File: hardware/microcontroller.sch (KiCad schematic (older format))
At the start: 9 parts, among them U1 ESP-WROOM-32

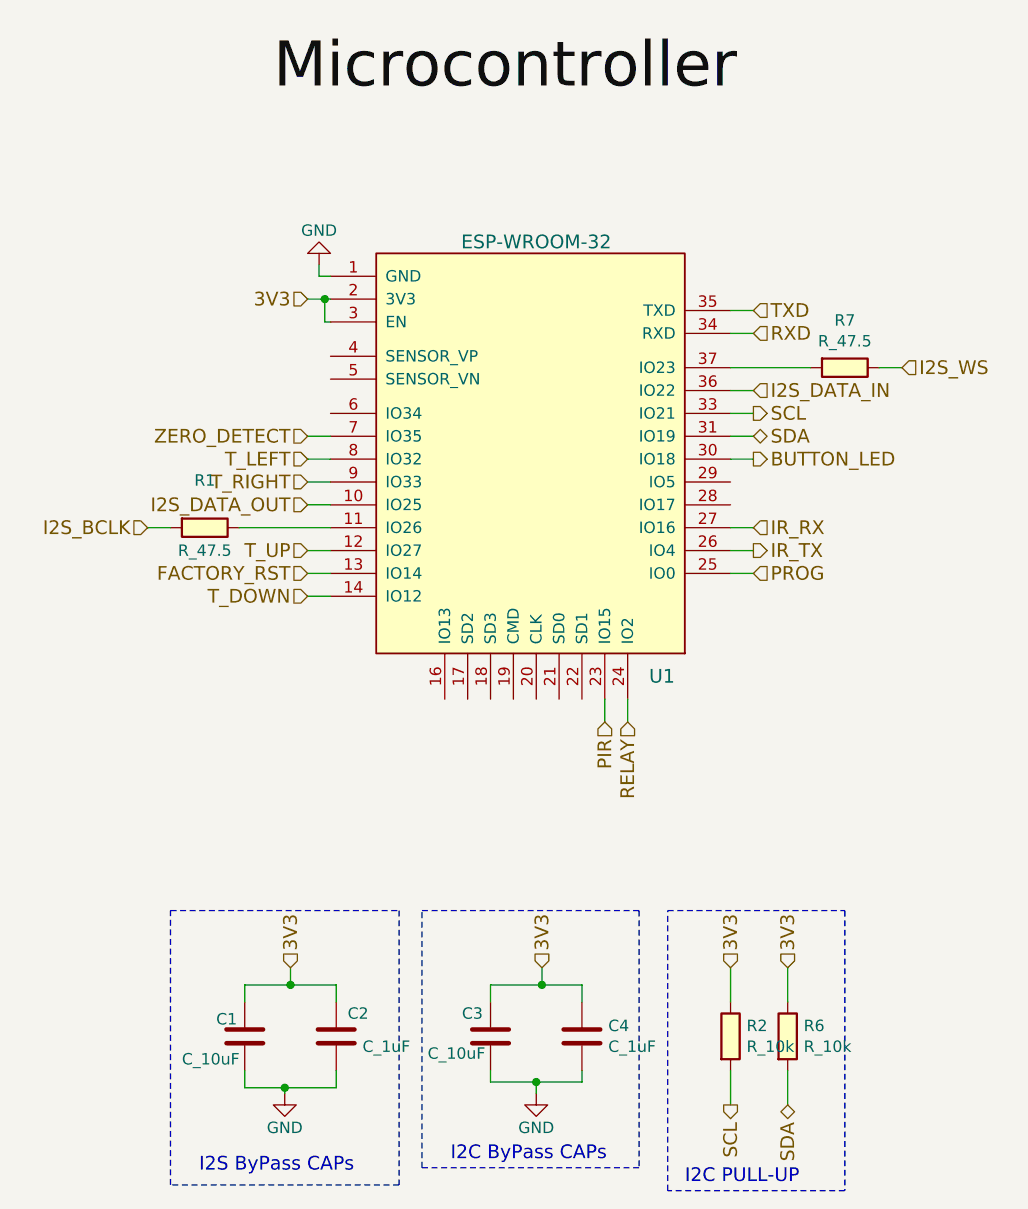
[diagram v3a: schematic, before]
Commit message: update schematic
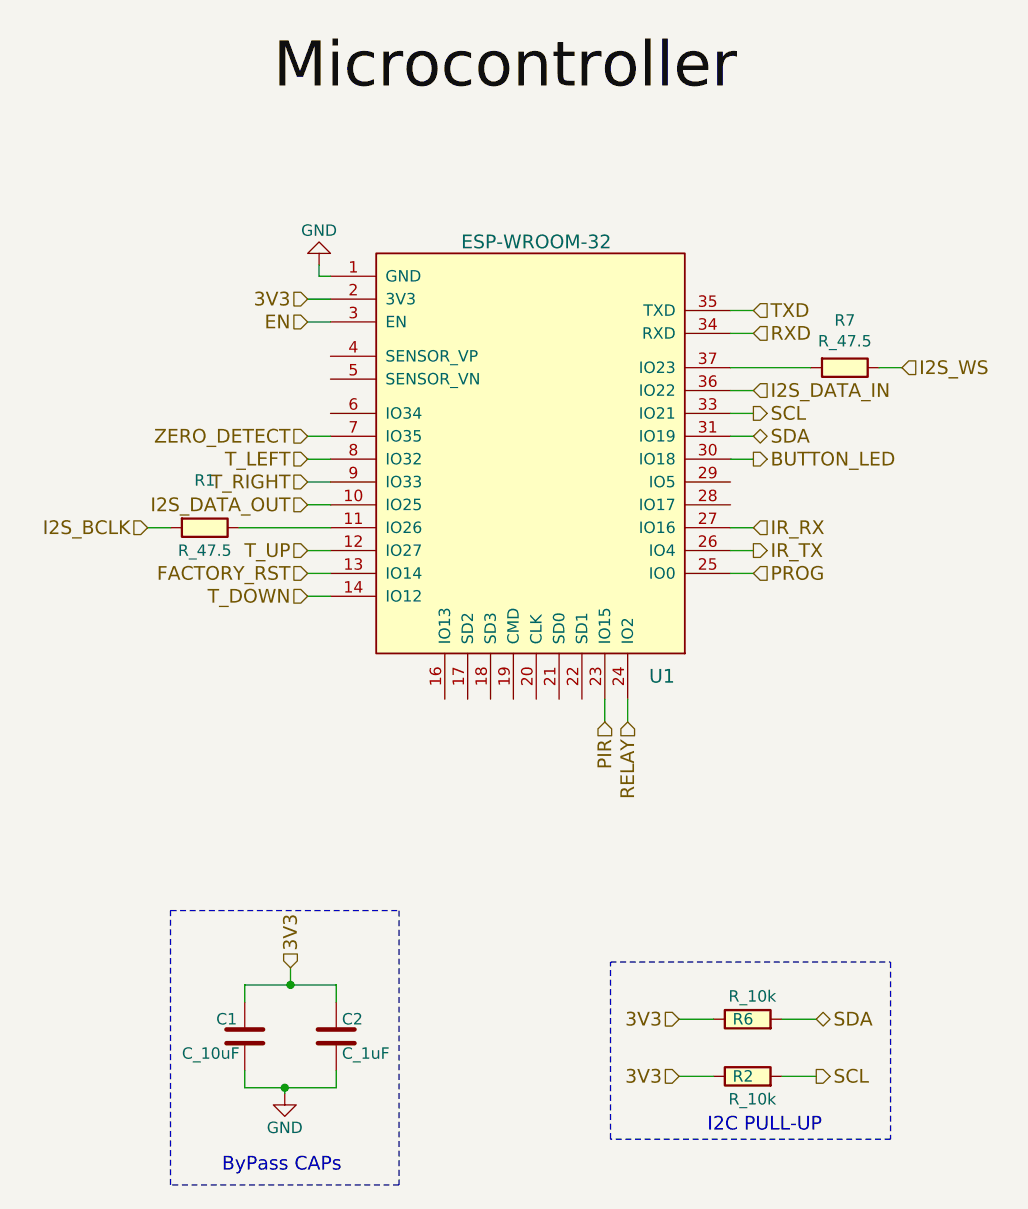
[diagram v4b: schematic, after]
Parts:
- removed C3: C_10uF, Capacitor_SMD:C_0603_1608Metric_Pad1.05x0.95mm_HandSolder, symbol open-automation:C_10uF
- removed C4: C_1uF, Capacitor_SMD:C_0603_1608Metric_Pad1.05x0.95mm_HandSolder, symbol open-automation:C_1uF
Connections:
- net 3V3: no longer U1.3 (EN)
- new net EN: U1.3 (EN)
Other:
- note added: "ByPass CAPs"
- note removed: "I2C ByPass CAPs"
- note removed: "I2S ByPass CAPs"
- moved on the sheet: R2, R6
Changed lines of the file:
@@
 	-1   0    0    1
-$EndComp
-$Comp
-L liger-rescue:ESP-WROOM-32 U1
-U 1 1 590979AF
-P 5950 2500
-F 0 "U1" H 6500 1400 60  0000 C CNN
-F 1 "ESP-WROOM-32" H 5950 3300 60  0000 C CNN
-F 2 "open-automation:ESP-WROOM-32" H 5600 3100 60  0001 C CNN
-F 3 "http://espressif.com/sites/default/files/documentation/esp-wroom-32_datasheet_en.pdf" H 5600 3100 60  0001 C CNN
-	1    5950 2500
-	1    0    0    -1
 $EndComp
 Text Label 4800 1075 0    197  ~ 0
 Microcontroller
-$Comp
-L power:GND #PWR02
-U 1 1 59C84AFB
-P 5950 5425
-F 0 "#PWR02" H 5950 5175 50  0001 C CNN
-F 1 "GND" H 5950 5275 50  0000 C CNN
-F 2 "" H 5950 5425 50  0000 C CNN
-F 3 "" H 5950 5425 50  0000 C CNN
-	1    5950 5425
-	1    0    0    -1
-$EndComp
-Text Notes 5575 5725 0    60   ~ 0
-I2C ByPass CAPs
 Wire Wire Line
 	4950 3150 5050 3150
@@
 Wire Wire Line
 	6350 3700 6350 3800
-Connection ~ 5950 5375
-Wire Wire Line
-	5950 5425 5950 5375
-Wire Wire Line
-	6150 5375 6150 5325
-Wire Wire Line
-	5750 5375 5950 5375
-Wire Wire Line
-	5750 5325 5750 5375
 Wire Wire Line
 	4250 2950 4350 2950
@@
 	7150 2250 6800 2250
 Wire Wire Line
-	7050 5025 7050 4875
-Wire Wire Line
-	6800 4875 6800 5025
-Wire Wire Line
-	6800 5325 6800 5475
-Wire Wire Line
-	7050 5325 7050 5475
+	6725 5100 6575 5100
+Wire Wire Line
+	6575 5350 6725 5350
+Wire Wire Line
+	7025 5350 7175 5350
+Wire Wire Line
+	7025 5100 7175 5100
 Wire Wire Line
 	6900 2350 6800 2350
@@
 Wire Wire Line
 	6800 3150 6900 3150
-Wire Wire Line
-	5050 1950 5025 1950
 Wire Wire Line
 	5000 1850 5050 1850
@@
 	1    0    0    -1
 $EndComp
-Text Notes 4475 5775 0    60   ~ 0
-I2S ByPass CAPs
+Text Notes 4575 5775 0    60   ~ 0
+ByPass CAPs
 Connection ~ 4850 5400
 Wire Wire Line
@@
 Wire Notes Line
 	5350 4625 5350 5825
-Wire Wire Line
-	5750 5025 5750 4950
-Wire Wire Line
-	5750 4950 5975 4950
-Wire Wire Line
-	6150 4950 6150 5025
-Wire Wire Line
-	5975 4875 5975 4950
-Connection ~ 5975 4950
-Wire Notes Line
-	5450 5750 6400 5750
-Wire Notes Line
-	5450 5750 5450 4625
-Wire Notes Line
-	5450 4625 6400 4625
-Wire Notes Line
-	6400 4625 6400 5750
-Text Notes 6600 5825 0    60   ~ 0
+Text Notes 7200 5600 2    60   ~ 0
 I2C PULL-UP
 Wire Notes Line
-	7300 5850 6525 5850
-Wire Notes Line
-	6525 5850 6525 4625
-Wire Notes Line
-	6525 4625 7300 4625
-Wire Notes Line
-	7300 4625 7300 5850
-Wire Wire Line
-	5950 5375 6150 5375
+	7500 4850 7500 5625
+Wire Notes Line
+	7500 5625 6275 5625
+Wire Notes Line
+	6275 5625 6275 4850
+Wire Notes Line
+	6275 4850 7500 4850
 Wire Wire Line
 	4850 5400 4675 5400
 Wire Wire Line
 	4875 4950 4675 4950
-Wire Wire Line
-	5975 4950 6150 4950
 Text HLabel 4950 1950 0    60   Input ~ 0
 3V3
-Wire Wire Line
-	5050 2050 5025 2050
-Wire Wire Line
-	5025 2050 5025 1950
-Connection ~ 5025 1950
-Wire Wire Line
-	5025 1950 4950 1950
 Text HLabel 4950 2650 0    60   Input ~ 0
 T_LEFT
@@
 Text HLabel 4875 4875 1    60   Input ~ 0
 3V3
-Text HLabel 5975 4875 1    60   Input ~ 0
-3V3
-Text HLabel 6800 4875 1    60   Input ~ 0
-3V3
-Text HLabel 7050 4875 1    60   Input ~ 0
-3V3
-Text HLabel 6800 5475 3    60   Output ~ 0
+Text HLabel 6575 5350 0    60   Input ~ 0
+3V3
+Text HLabel 6575 5100 0    60   Input ~ 0
+3V3
+Text HLabel 7175 5350 2    60   Output ~ 0
 SCL
-Text HLabel 7050 5475 3    60   BiDi ~ 0
+Text HLabel 7175 5100 2    60   BiDi ~ 0
 SDA
-$Comp
-L open-automation:C_1uF C4
-U 1 1 5B1F1AAD
-P 6150 5175
-F 0 "C4" H 6265 5221 50  0000 L CNN
-F 1 "C_1uF" H 6265 5130 50  0000 L CNN
-F 2 "Capacitor_SMD:C_0603_1608Metric_Pad1.05x0.95mm_HandSolder" H 6250 5475 50  0001 C CNN
-F 3 "https://www.digikey.com/product-detail/en/tdk-corporation/CGA3E1X7R1C105M080AC/445-12540-1-ND/3954206" H 6150 4925 50  0001 C CNN
-F 4 "CL10B105KP8NNNC" H 6275 5375 60  0001 C CNN "Part Number"
-	1    6150 5175
-	1    0    0    -1
-$EndComp
 $Comp
 L open-automation:C_1uF C2
 U 1 1 5B1F1B60
 P 5075 5175
-F 0 "C2" H 5125 5275 50  0000 L CNN
-F 1 "C_1uF" H 5190 5130 50  0000 L CNN
+F 0 "C2" H 5100 5250 50  0000 L CNN
+F 1 "C_1uF" H 5100 5100 50  0000 L CNN
 F 2 "Capacitor_SMD:C_0603_1608Metric_Pad1.05x0.95mm_HandSolder" H 5175 5475 50  0001 C CNN
 F 3 "https://www.digikey.com/product-detail/en/tdk-corporation/CGA3E1X7R1C105M080AC/445-12540-1-ND/3954206" H 5075 4925 50  0001 C CNN
@@
 $EndComp
 $Comp
-L open-automation:C_10uF C3
-U 1 1 5B1F217F
-P 5750 5175
-F 0 "C3" H 5625 5275 50  0000 L CNN
-F 1 "C_10uF" H 5475 5100 50  0000 L CNN
-F 2 "Capacitor_SMD:C_0603_1608Metric_Pad1.05x0.95mm_HandSolder" H 5850 5475 50  0001 C CNN
-F 3 "https://www.digikey.com/product-detail/en/samsung-electro-mechanics/CL10A106MP8NNNC/1276-1871-1-ND/3889957" H 5750 4925 50  0001 C CNN
-F 4 "CL10A106MP8NNNC" H 5875 5375 60  0001 C CNN "Part Number"
-	1    5750 5175
-	1    0    0    -1
-$EndComp
-$Comp
 L open-automation:C_10uF C1
 U 1 1 5B1F22B0
 P 4675 5175
 F 0 "C1" H 4550 5250 50  0000 L CNN
-F 1 "C_10uF" H 4400 5075 50  0000 L CNN
+F 1 "C_10uF" H 4400 5100 50  0000 L CNN
 F 2 "Capacitor_SMD:C_0603_1608Metric_Pad1.05x0.95mm_HandSolder" H 4775 5475 50  0001 C CNN
 F 3 "https://www.digikey.com/product-detail/en/samsung-electro-mechanics/CL10A106MP8NNNC/1276-1871-1-ND/3889957" H 4675 4925 50  0001 C CNN
@@
 L open-automation:R_10k R6
 U 1 1 5B31EE0D
-P 7050 5175
-F 0 "R6" H 7120 5221 50  0000 L CNN
-F 1 "R_10k" H 7120 5130 50  0000 L CNN
-F 2 "Resistor_SMD:R_0603_1608Metric_Pad1.05x0.95mm_HandSolder" V 6980 5175 50  0001 C CNN
-F 3 "https://www.digikey.com/product-detail/en/yageo/RC0603JR-0710KL/311-10KGRCT-ND/729647" V 7130 5175 50  0001 C CNN
-F 4 "MCT06030C1002FP500" V 7230 5275 60  0001 C CNN "Part Number"
-	1    7050 5175
-	1    0    0    -1
+P 6875 5100
+F 0 "R6" V 6875 5075 50  0000 L CNN
+F 1 "R_10k" V 6975 4975 50  0000 L CNN
+F 2 "Resistor_SMD:R_0603_1608Metric_Pad1.05x0.95mm_HandSolder" V 6805 5100 50  0001 C CNN
+F 3 "https://www.digikey.com/product-detail/en/yageo/RC0603JR-0710KL/311-10KGRCT-ND/729647" V 6955 5100 50  0001 C CNN
+F 4 "MCT06030C1002FP500" V 7055 5200 60  0001 C CNN "Part Number"
+	1    6875 5100
+	0    -1   -1   0
 $EndComp
 $Comp
 L open-automation:R_10k R2
 U 1 1 5B31EE98
-P 6800 5175
-F 0 "R2" H 6870 5221 50  0000 L CNN
-F 1 "R_10k" H 6870 5130 50  0000 L CNN
-F 2 "Resistor_SMD:R_0603_1608Metric_Pad1.05x0.95mm_HandSolder" V 6730 5175 50  0001 C CNN
-F 3 "https://www.digikey.com/product-detail/en/yageo/RC0603JR-0710KL/311-10KGRCT-ND/729647" V 6880 5175 50  0001 C CNN
-F 4 "MCT06030C1002FP500" V 6980 5275 60  0001 C CNN "Part Number"
-	1    6800 5175
-	1    0    0    -1
+P 6875 5350
+F 0 "R2" V 6875 5325 50  0000 L CNN
+F 1 "R_10k" V 6775 5225 50  0000 L CNN
+F 2 "Resistor_SMD:R_0603_1608Metric_Pad1.05x0.95mm_HandSolder" V 6805 5350 50  0001 C CNN
+F 3 "https://www.digikey.com/product-detail/en/yageo/RC0603JR-0710KL/311-10KGRCT-ND/729647" V 6955 5350 50  0001 C CNN
+F 4 "MCT06030C1002FP500" V 7055 5450 60  0001 C CNN "Part Number"
+	1    6875 5350
+	0    -1   -1   0
 $EndComp
 $Comp
@@
 Text HLabel 4950 2550 0    60   Input ~ 0
 ZERO_DETECT
+$Comp
+L liger-rescue:ESP-WROOM-32 U1
+U 1 1 590979AF
+P 5950 2500
+F 0 "U1" H 6500 1400 60  0000 C CNN
+F 1 "ESP-WROOM-32" H 5950 3300 60  0000 C CNN
+F 2 "open-automation:ESP-WROOM-32" H 5600 3100 60  0001 C CNN
+F 3 "http://espressif.com/sites/default/files/documentation/esp-wroom-32_datasheet_en.pdf" H 5600 3100 60  0001 C CNN
+	1    5950 2500
+	1    0    0    -1
+$EndComp
+Text HLabel 4950 2050 0    60   Input ~ 0
+EN
+Wire Wire Line
+	4950 1950 5050 1950
+Wire Wire Line
+	4950 2050 5050 2050
 $EndSCHEMATC

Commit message: send board to board house, v0.7.2
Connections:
- net RELAY_3: now reaches U1.28 (IO17)
- net RELAY_2: now reaches U1.29 (IO5)
- net RELAY_4: now reaches U1.6 (IO34)
- net RELAY renamed RELAY_1
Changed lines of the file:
@@
 EESchema Schematic File Version 4
 LIBS:liger-cache
-EELAYER 26 0
+EELAYER 29 0
 EELAYER END
 $Descr A4 11693 8268
 encoding utf-8
-Sheet 2 9
+Sheet 2 8
 Title ""
 Date ""
@@
 PIR
 Text HLabel 6350 3800 3    60   Input ~ 0
-RELAY
+RELAY_1
 Text HLabel 6900 3150 2    60   Input ~ 0
 PROG
@@
 Wire Wire Line
 	4950 2050 5050 2050
+Text HLabel 6825 2750 2    60   Input ~ 0
+RELAY_2
+Wire Wire Line
+	6825 2750 6800 2750
+Text HLabel 6825 2850 2    60   Input ~ 0
+RELAY_3
+Wire Wire Line
+	6825 2850 6800 2850
+Text HLabel 5000 2450 0    60   Input ~ 0
+RELAY_4
+Wire Wire Line
+	5000 2450 5050 2450
 $EndSCHEMATC
